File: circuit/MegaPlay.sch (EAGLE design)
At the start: 13 parts, among them IC1 4052N, IC2 4052N, M1 ARDUINO-NANO-3.0, X1 Mega, X2 5200

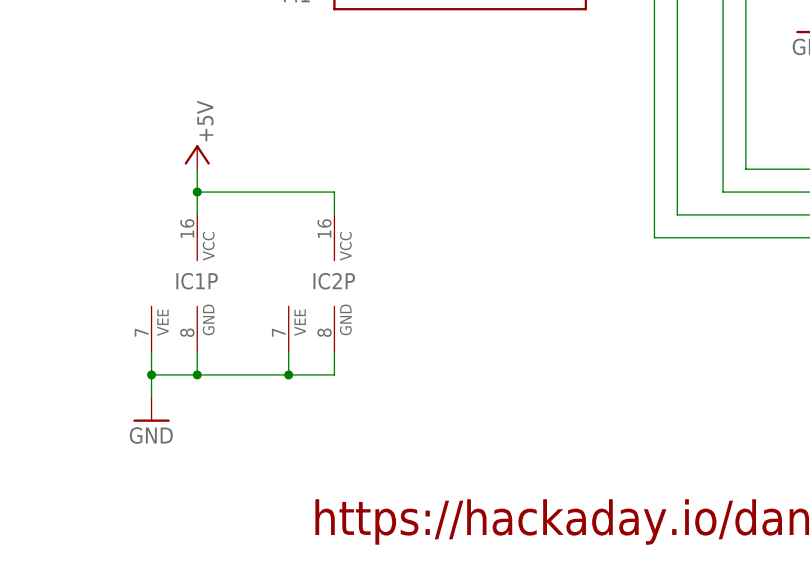
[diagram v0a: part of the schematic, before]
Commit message: Added decoupling capacitor to Analog Switches power supply.
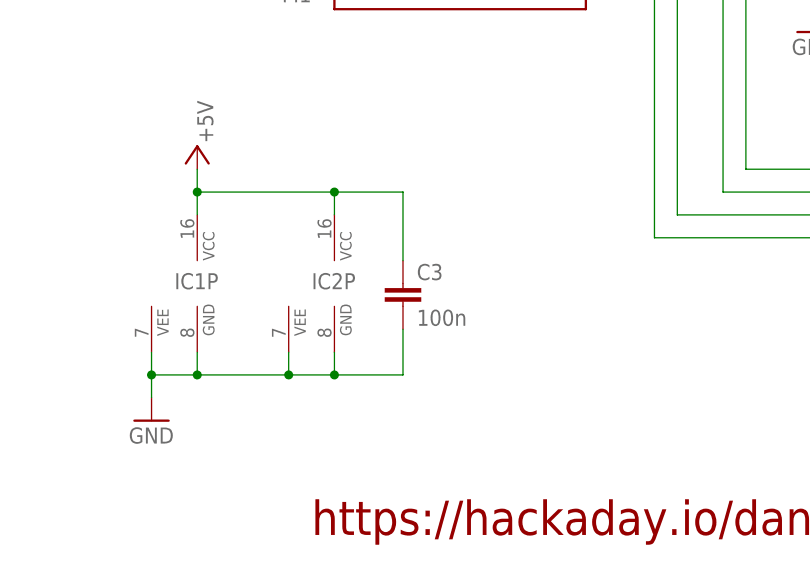
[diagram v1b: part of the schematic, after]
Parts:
- added C3: 100n, rcl:C-EU050-024X044
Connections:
- net +5V: now also C3.1
- net GND: now also C3.2
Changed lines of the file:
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@@
 <grid distance="0.1" unitdist="inch" unit="inch" style="lines" multiple="1" display="no" altdistance="0.01" altunitdist="inch" altunit="inch"/>
 <layers>
-<layer number="1" name="Top" color="4" fill="9" visible="no" active="no"/>
-<layer number="16" name="Bottom" color="1" fill="1" visible="no" active="no"/>
-<layer number="17" name="Pads" color="2" fill="1" visible="no" active="no"/>
-<layer number="18" name="Vias" color="2" fill="1" visible="no" active="no"/>
-<layer number="19" name="Unrouted" color="6" fill="1" visible="no" active="no"/>
-<layer number="20" name="Dimension" color="15" fill="1" visible="no" active="no"/>
-<layer number="21" name="tPlace" color="7" fill="1" visible="no" active="no"/>
-<layer number="22" name="bPlace" color="7" fill="1" visible="no" active="no"/>
-<layer number="23" name="tOrigins" color="15" fill="1" visible="no" active="no"/>
-<layer number="24" name="bOrigins" color="15" fill="1" visible="no" active="no"/>
-<layer number="25" name="tNames" color="7" fill="1" visible="no" active="no"/>
-<layer number="26" name="bNames" color="7" fill="1" visible="no" active="no"/>
-<layer number="27" name="tValues" color="7" fill="1" visible="no" active="no"/>
-<layer number="28" name="bValues" color="7" fill="1" visible="no" active="no"/>
+<layer number="1" name="Top" color="4" fill="1" visible="yes" active="no"/>
+<layer number="16" name="Bottom" color="1" fill="1" visible="yes" active="no"/>
+<layer number="17" name="Pads" color="2" fill="1" visible="yes" active="no"/>
+<layer number="18" name="Vias" color="2" fill="1" visible="yes" active="no"/>
+<layer number="19" name="Unrouted" color="6" fill="1" visible="yes" active="no"/>
+<layer number="20" name="Dimension" color="15" fill="1" visible="yes" active="no"/>
+<layer number="21" name="tPlace" color="7" fill="1" visible="yes" active="no"/>
+<layer number="22" name="bPlace" color="7" fill="1" visible="yes" active="no"/>
+<layer number="23" name="tOrigins" color="15" fill="1" visible="yes" active="no"/>
+<layer number="24" name="bOrigins" color="15" fill="1" visible="yes" active="no"/>
+<layer number="25" name="tNames" color="7" fill="1" visible="yes" active="no"/>
+<layer number="26" name="bNames" color="7" fill="1" visible="yes" active="no"/>
+<layer number="27" name="tValues" color="7" fill="1" visible="yes" active="no"/>
+<layer number="28" name="bValues" color="7" fill="1" visible="yes" active="no"/>
 <layer number="29" name="tStop" color="7" fill="3" visible="no" active="no"/>
 <layer number="30" name="bStop" color="7" fill="6" visible="no" active="no"/>
@@
 <layer number="35" name="tGlue" color="7" fill="4" visible="no" active="no"/>
 <layer number="36" name="bGlue" color="7" fill="5" visible="no" active="no"/>
-<layer number="37" name="tTest" color="7" fill="1" visible="no" active="no"/>
-<layer number="38" name="bTest" color="7" fill="1" visible="no" active="no"/>
+<layer number="37" name="tTest" color="7" fill="1" visible="yes" active="no"/>
+<layer number="38" name="bTest" color="7" fill="1" visible="yes" active="no"/>
 <layer number="39" name="tKeepout" color="4" fill="11" visible="no" active="no"/>
 <layer number="40" name="bKeepout" color="1" fill="11" visible="no" active="no"/>
@@
 <layer number="44" name="Drills" color="7" fill="1" visible="no" active="no"/>
 <layer number="45" name="Holes" color="7" fill="1" visible="no" active="no"/>
-<layer number="46" name="Milling" color="3" fill="1" visible="no" active="no"/>
-<layer number="47" name="Measures" color="7" fill="1" visible="no" active="no"/>
-<layer number="48" name="Document" color="7" fill="1" visible="no" active="no"/>
-<layer number="49" name="Reference" color="7" fill="1" visible="no" active="no"/>
-<layer number="50" name="dxf" color="7" fill="1" visible="no" active="no"/>
-<layer number="51" name="tDocu" color="7" fill="1" visible="no" active="no"/>
-<layer number="52" name="bDocu" color="7" fill="1" visible="no" active="no"/>
-<layer number="53" name="tGND_GNDA" color="7" fill="9" visible="no" active="no"/>
-<layer number="54" name="bGND_GNDA" color="1" fill="9" visible="no" active="no"/>
-<layer number="56" name="wert" color="7" fill="1" visible="no" active="no"/>
-<layer number="57" name="tCAD" color="7" fill="1" visible="no" active="no"/>
-<layer number="59" name="tCarbon" color="7" fill="1" visible="no" active="no"/>
-<layer number="60" name="bCarbon" color="7" fill="1" visible="no" active="no"/>
+<layer number="46" name="Milling" color="3" fill="1" visible="yes" active="no"/>
+<layer number="47" name="Measures" color="7" fill="1" visible="yes" active="no"/>
+<layer number="48" name="Document" color="7" fill="1" visible="yes" active="no"/>
+<layer number="49" name="Reference" color="7" fill="1" visible="yes" active="no"/>
+<layer number="50" name="dxf" color="7" fill="1" visible="yes" active="no"/>
+<layer number="51" name="tDocu" color="7" fill="1" visible="yes" active="no"/>
+<layer number="52" name="bDocu" color="7" fill="1" visible="yes" active="no"/>
+<layer number="53" name="tGND_GNDA" color="7" fill="9" visible="yes" active="no"/>
+<layer number="54" name="bGND_GNDA" color="1" fill="9" visible="yes" active="no"/>
+<layer number="56" name="wert" color="7" fill="1" visible="yes" active="no"/>
+<layer number="57" name="tCAD" color="7" fill="1" visible="yes" active="no"/>
+<layer number="59" name="tCarbon" color="7" fill="1" visible="yes" active="no"/>
+<layer number="60" name="bCarbon" color="7" fill="1" visible="yes" active="no"/>
 <layer number="90" name="Modules" color="5" fill="1" visible="yes" active="yes"/>
 <layer number="91" name="Nets" color="2" fill="1" visible="yes" active="yes"/>
@@
 <part name="D1" library="diode" deviceset="ZENER-DIODE" device="ZD-7.5" value="5V1"/>
 <part name="FRAME1" library="frames" deviceset="A4L-LOC" device=""/>
+<part name="C3" library="rcl" deviceset="C-EU" device="050-024X044" value="100n"/>
 </parts>
 <sheets>
@@
 <instance part="D1" gate="G$1" x="111.76" y="83.82" rot="R90"/>
 <instance part="FRAME1" gate="G$1" x="0" y="0"/>
+<instance part="C3" gate="G$1" x="66.04" y="38.1"/>
 </instances>
 <busses>
@@
 <wire x1="58.42" y1="27.94" x2="58.42" y2="30.48" width="0.1524" layer="91"/>
 <junction x="53.34" y="27.94"/>
+<pinref part="C3" gate="G$1" pin="2"/>
+<wire x1="58.42" y1="27.94" x2="66.04" y2="27.94" width="0.1524" layer="91"/>
+<wire x1="66.04" y1="27.94" x2="66.04" y2="33.02" width="0.1524" layer="91"/>
+<junction x="58.42" y="27.94"/>
 </segment>
 <segment>
@@
 <wire x1="58.42" y1="48.26" x2="58.42" y2="45.72" width="0.1524" layer="91"/>
 <junction x="43.18" y="48.26"/>
+<pinref part="C3" gate="G$1" pin="1"/>
+<wire x1="58.42" y1="48.26" x2="66.04" y2="48.26" width="0.1524" layer="91"/>
+<wire x1="66.04" y1="48.26" x2="66.04" y2="40.64" width="0.1524" layer="91"/>
+<junction x="58.42" y="48.26"/>
 </segment>
 </net>
